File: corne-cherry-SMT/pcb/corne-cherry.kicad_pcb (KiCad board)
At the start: 2 copper layers, 274.5 x 91.9 mm, 140 parts, among them J1 MJ-4PP-9, J2 OLED, J3 MJ-4PP-9, J4 OLED, J5 Conn_01x02, J6 Conn_01x02, J7 Conn_01x05_MountingPin, J8 Conn_01x05_MountingPin, SW1 SW_PUSH, SW10 SW_PUSH, SW11 SW_PUSH, SW12 SW_PUSH, SW13 SW_PUSH, SW14 SW_PUSH, SW15 SW_PUSH, SW16 SW_PUSH, SW17 SW_PUSH, SW18 SW_PUSH, SW19 SW_PUSH, SW2 SW_PUSH, SW20 SW_PUSH, SW21 SW_PUSH, SW22 SW_PUSH, SW23 SW_PUSH, SW24 SW_PUSH, SW25 SW_PUSH, SW26 SW_PUSH, SW27 SW_PUSH, SW28 SW_PUSH, SW29 SW_PUSH, SW3 SW_PUSH, SW30 SW_PUSH, SW31 SW_PUSH, SW32 SW_PUSH, SW33 SW_PUSH, SW34 SW_PUSH, SW35 SW_PUSH, SW36 SW_PUSH, SW37 SW_PUSH, SW38 SW_PUSH, SW39 SW_PUSH, SW4 SW_PUSH, SW40 SW_PUSH, SW41 SW_PUSH, SW42 SW_PUSH, SW43 SW_PUSH, SW44 SW_PUSH, SW5 SW_PUSH, SW6 SW_PUSH, SW7 SW_PUSH, SW8 SW_PUSH, SW9 SW_PUSH, U2 ProMicro, U3 ProMicro_r

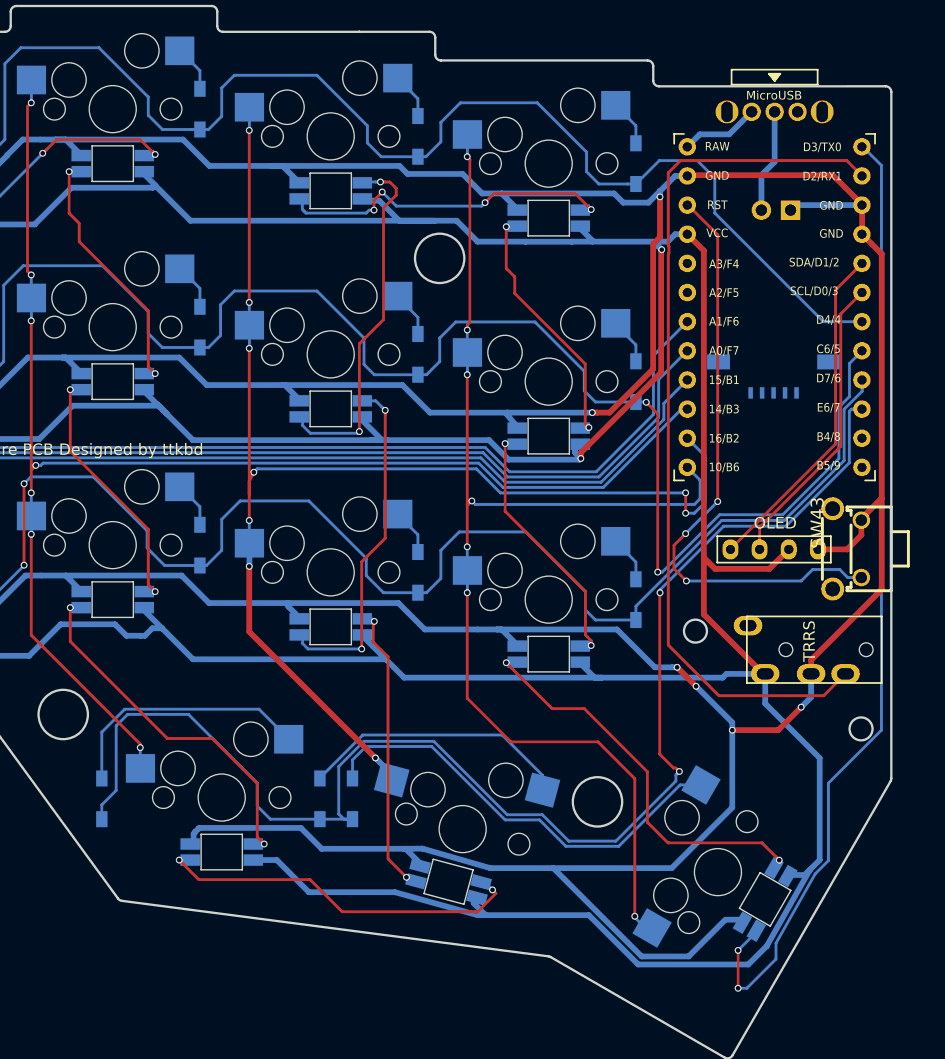
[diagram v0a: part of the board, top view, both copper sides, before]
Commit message: add rotate encoder in the left
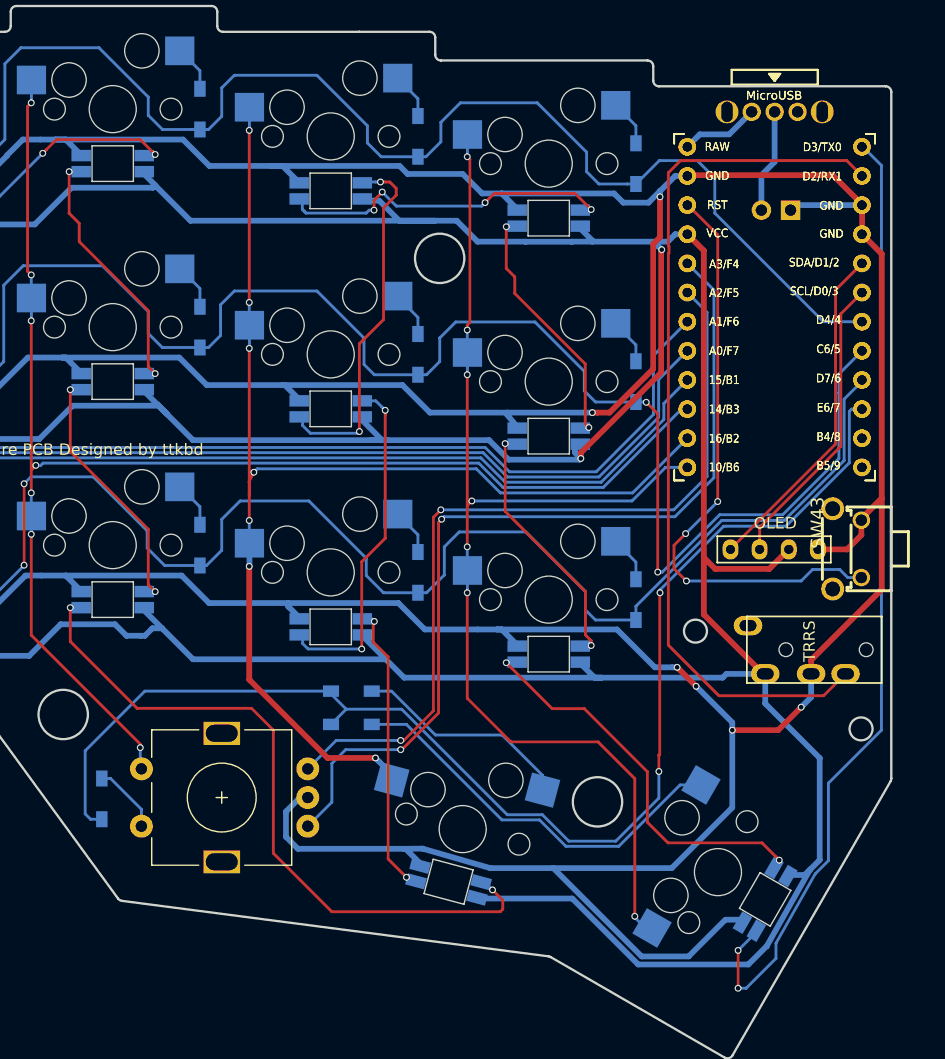
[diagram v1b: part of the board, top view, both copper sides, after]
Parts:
- removed J7: Conn_01x05_MountingPin, Connector_FFC-FPC:Molex_200528-0050_1x05-1MP_P1.00mm_Horizontal
- removed LED25: YS-SK6812MINI-E, kbd:YS-SK6812MINI-E
- removed SW19: SW_PUSH, kbd:CherryMX_Hotswap
- added SW45: Rotary_Encoder_Switch, SofleKeyboard-footprint:RotaryEncoder_Alps_EC11E-Switch_Vertical_H20mm-keebio_modified, F.Cu at (86.6, 88.7)
- added U2: ProMicro, kbd:ProMicro_v3, F.Cu at (134.8, 46.4)
- moved D20 9.78 mm to (97.9, 79.4), turned to 0 degrees
- moved D21 6.49 mm to (97.9, 82.3), turned to 0 degrees
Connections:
- net col3 renamed SW19A
- D19 pad 2: Net-(D19-A) -> SW19B
- LED26 pad 2: Net-(LED25-DIN) -> Net-(LED22-DIN)
- U2 pad 19: joystickY -> EncoderB
- U2 pad 20: joystickX -> EncoderA
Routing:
- net EncoderA: track 0.00 -> 79.3 mm, vias 0 -> 2
- net EncoderB: track 0.00 -> 72.0 mm, vias 0 -> 2
- net Net-(LED25-DIN): track 33.5 -> 0.00 mm, vias 2 -> 0
- net Net-(LED22-DIN): track 32.4 -> 61.7 mm
- net VCC: track 533.9 -> 510.8 mm
- net Net-(D19-A): track 22.3 -> 0.00 mm
- net row3: track 120.7 -> 113.2 mm
- net SW19B: track 0.00 -> 6.04 mm
- net col4: track 114.7 -> 109.1 mm, vias 9 -> 7
- net GND: track 578.5 -> 573.6 mm
- net Net-(D20-A): track 23.7 -> 19.2 mm
- net col5: track 105.0 -> 101.5 mm
- net Net-(D21-A): track 38.3 -> 35.3 mm
